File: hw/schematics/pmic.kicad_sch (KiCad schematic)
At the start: 40 parts, among them J1 TYPE-C-31-M-13C, J2 Conn_01x02, U2 NPM1300-QEAA-R

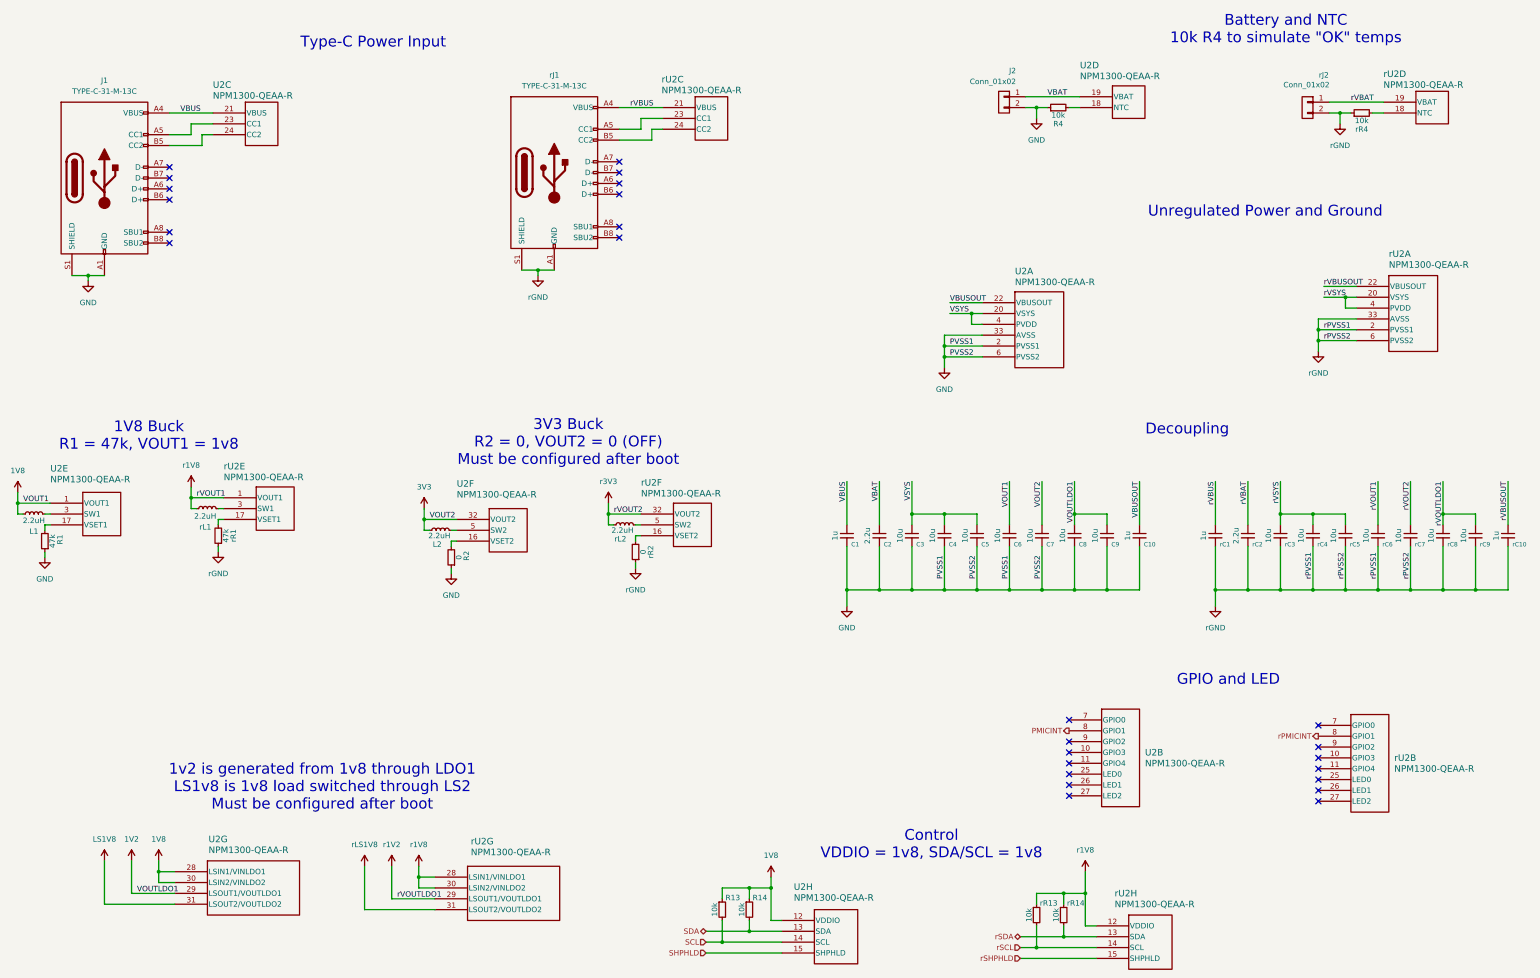
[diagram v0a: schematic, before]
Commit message: Annotate; Remove unused LDO/LS; Add RGB LED to PMIC
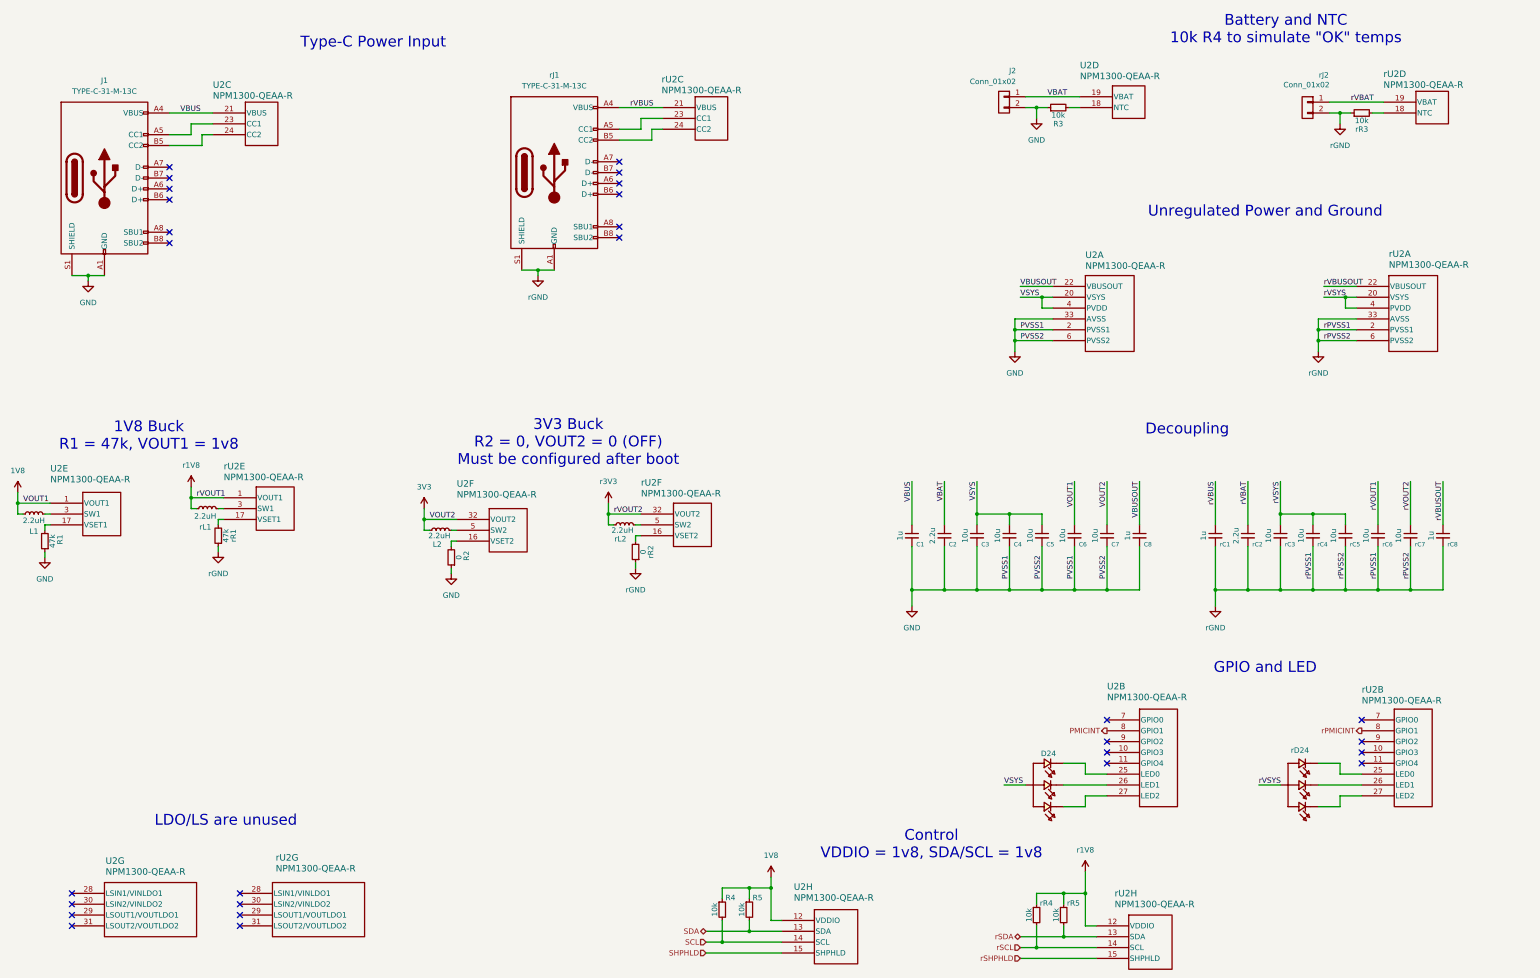
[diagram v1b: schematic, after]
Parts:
- removed C8, C9, rC8, rC9: 10u, Alidade:0603, symbol Alidade:C
- added D24, rD24: LED_RGB_COM_ANODE, symbol Alidade:LED_RGB_COM_ANODE
- renumbered C10 to C8, R4 to R3, R13 to R4, R14 to R5, rC10 to rC8, rR4 to rR3, rR13 to rR4, rR14 to rR5
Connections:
- net 1V8: no longer U2.28 (LSIN1/VINLDO1), U2.30 (LSIN2/VINLDO2)
- net VSYS: now also D24.4
- net r1V8: no longer rU2.28 (LSIN1/VINLDO1), rU2.30 (LSIN2/VINLDO2)
- net rVSYS: now also rD24.4
- net at U2.25 (LED0): now also D24.1 (R)
- net at U2.26 (LED1): now also D24.2 (G)
- net at U2.27 (LED2): now also D24.3 (B)
- net at rU2.25 (LED0): now also rD24.1 (R)
- net at rU2.26 (LED1): now also rD24.2 (G)
- net at rU2.27 (LED2): now also rD24.3 (B)
- net 1V2: no longer names the net of U2.29 (LSOUT1/VOUTLDO1)
- net LS1V8: no longer names the net of U2.31 (LSOUT2/VOUTLDO2)
- net r1V2: no longer names the net of rU2.29 (LSOUT1/VOUTLDO1)
- net rLS1V8: no longer names the net of rU2.31 (LSOUT2/VOUTLDO2)
- no-connect marks 26 -> 28
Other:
- note added: "LDO/LS are unused"
- note removed: "1v2 is generated from 1v8 through LDO1 LS1v8 is 1v8 load switched through LS2 Must be configured after boot"
- moved on the sheet: C1, C2, C3, C4, C5, C6, C7, U2A, U2B, U2G, rC8, rU2B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

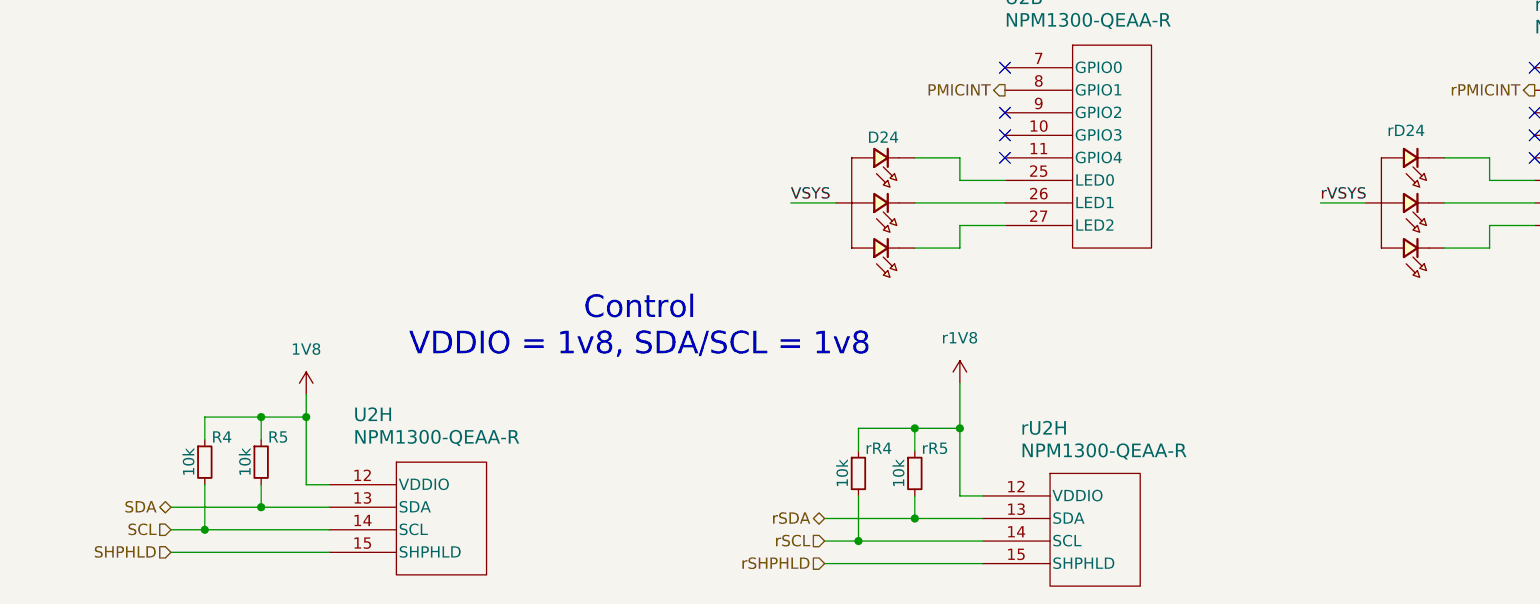
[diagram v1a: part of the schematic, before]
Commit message: Place shphld switches
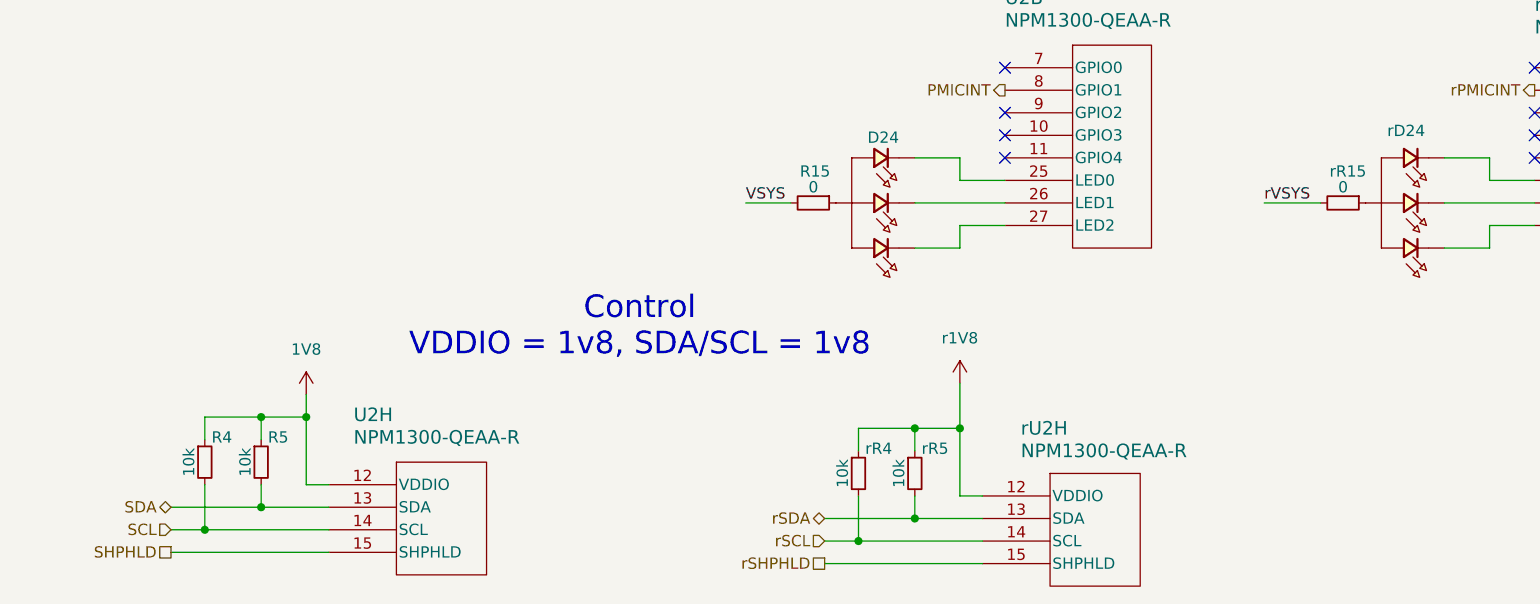
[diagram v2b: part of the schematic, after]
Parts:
- added R15, rR15: 0, Alidade:0603, symbol Alidade:R
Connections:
- net VSYS: now also R15.2; no longer D24.4
- net rVSYS: now also rR15.2; no longer rD24.4
- new net: rD24.4, rR15.1
- new net: D24.4, R15.1
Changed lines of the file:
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@@
 	(wire
 		(pts
+			(xy 266.7 207.01) (xy 271.78 207.01)
+		)
+		(stroke
+			(width 0)
+			(type default)
+		)
+	)
+	(wire
+		(pts
 			(xy 273.05 146.05) (xy 273.05 143.51)
 		)
@@
 	(wire
 		(pts
-			(xy 336.55 207.01) (xy 331.47 207.01)
-		)
-		(stroke
-			(width 0)
-			(type default)
-		)
-	)
-	(wire
-		(pts
 			(xy 142.24 156.21) (xy 142.24 157.48)
 		)
@@
 	(wire
 		(pts
-			(xy 276.86 207.01) (xy 271.78 207.01)
-		)
-		(stroke
-			(width 0)
-			(type default)
-		)
-	)
-	(wire
-		(pts
 			(xy 83.82 54.61) (xy 86.36 54.61)
 		)
@@
 	(wire
 		(pts
+			(xy 325.12 207.01) (xy 331.47 207.01)
+		)
+		(stroke
+			(width 0)
+			(type default)
+		)
+	)
+	(wire
+		(pts
 			(xy 76.2 49.53) (xy 86.36 49.53)
 		)
@@
 	)
 	(label "VSYS"
-		(at 271.78 207.01 0)
+		(at 266.7 207.01 0)
 		(effects
 			(font
@@
 	)
 	(label "rVSYS"
-		(at 331.47 207.01 0)
+		(at 325.12 207.01 0)
 		(effects
 			(font
@@
 	)
 	(hierarchical_label "SHPHLD"
-		(shape input)
+		(shape passive)
 		(at 201.93 246.38 180)
 		(effects
@@
 	)
 	(hierarchical_label "rSHPHLD"
-		(shape input)
+		(shape passive)
 		(at 275.59 247.65 180)
 		(effects
@@
 	(symbol
 		(lib_id "Alidade:R")
+		(at 274.32 207.01 270)
+		(unit 1)
+		(exclude_from_sim no)
+		(in_bom yes)
+		(on_board yes)
+		(dnp no)
+		(property "Reference" "R15"
+			(at 272.796 203.454 90)
+			(effects
+				(font
+					(size 1.27 1.27)
+				)
+				(justify left)
+			)
+		)
+		(property "Value" "0"
+			(at 274.32 205.232 90)
+			(do_not_autoplace yes)
+			(effects
+				(font
+					(size 1.27 1.27)
+				)
+			)
+		)
+		(property "Footprint" "Alidade:0603"
+			(at 274.32 207.01 0)
+			(effects
+				(font
+					(size 1.27 1.27)
+				)
+				(hide yes)
+			)
+		)
+		(property "Datasheet" ""
+			(at 274.32 207.01 0)
+			(effects
+				(font
+					(size 1.27 1.27)
+				)
+				(hide yes)
+			)
+		)
+		(property "Description" ""
+			(at 274.32 207.01 0)
+			(effects
+				(font
+					(size 1.27 1.27)
+				)
+				(hide yes)
+			)
+		)
+		(property "LCSC Part #" "C21189"
+			(at 274.32 207.01 90)
+			(effects
+				(font
+					(size 1.27 1.27)
+				)
+				(hide yes)
+			)
+		)
+		(pin "2"
+		)
+		(pin "1"
+		)
+		(instances
+			(project "alidade"
+				(path "/4cc5d416-57f5-4147-8183-e03ae6b1198a/29a12dcc-0491-44a2-8290-cbef7c573a8c"
+					(reference "R15")
+					(unit 1)
+				)
+			)
+		)
+	)
+	(symbol
+		(lib_id "Alidade:R")
 		(at 87.63 148.59 180)
 		(unit 1)
@@
 				)
 			)
+		)
+	)
+	(symbol
+		(lib_id "Alidade:R")
+		(at 334.01 207.01 270)
+		(unit 1)
+		(exclude_from_sim no)
+		(in_bom yes)
+		(on_board yes)
+		(dnp no)
+		(property "Reference" "rR15"
+			(at 332.486 203.454 90)
+			(effects
+				(font
+					(size 1.27 1.27)
+				)
+				(justify left)
+			)
+		)
+		(property "Value" "0"
+			(at 334.01 205.232 90)
+			(do_not_autoplace yes)
+			(effects
+				(font
+					(size 1.27 1.27)
+				)
+			)
+		)
+		(property "Footprint" "Alidade:0603"
+			(at 334.01 207.01 0)
+			(effects
+				(font
+					(size 1.27 1.27)
+				)
+				(hide yes)
+			)
+		)
+		(property "Datasheet" ""
+			(at 334.01 207.01 0)
+			(effects
+				(font
+					(size 1.27 1.27)
+				)
+				(hide yes)
+			)
+		)
+		(property "Description" ""
+			(at 334.01 207.01 0)
+			(effects
+				(font
+					(size 1.27 1.27)
+				)
+				(hide yes)
+			)
+		)
+		(property "LCSC Part #" "C21189"
+			(at 334.01 207.01 90)
+			(effects
+				(font
+					(size 1.27 1.27)
+				)
+				(hide yes)
+			)
+		)
+		(pin "2"
+		)
+		(pin "1"
+		)
+		(instances
+			(project "alidade"
+				(path "/4cc5d416-57f5-4147-8183-e03ae6b1198a/29a12dcc-0491-44a2-8290-cbef7c573a8c"
+					(reference "rR15")
+					(unit 1)
+				)
+			)
